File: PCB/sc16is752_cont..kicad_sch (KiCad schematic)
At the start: 57 parts, among them IC13 SN74LVC1G125DBVT, IC14 LM3940IMP-3.3_NOPB, IC15 SN74LVC1G125DBVT, IC16 AP63205WU-7, J3 5747842-2, J4 Screw_Terminal_01x02, J5 Screw_Terminal_01x02, J6 5747842-2, Q1 SI2307CDS-T1-GE3, Y2 ASE-14.7456MHZ-LC-T

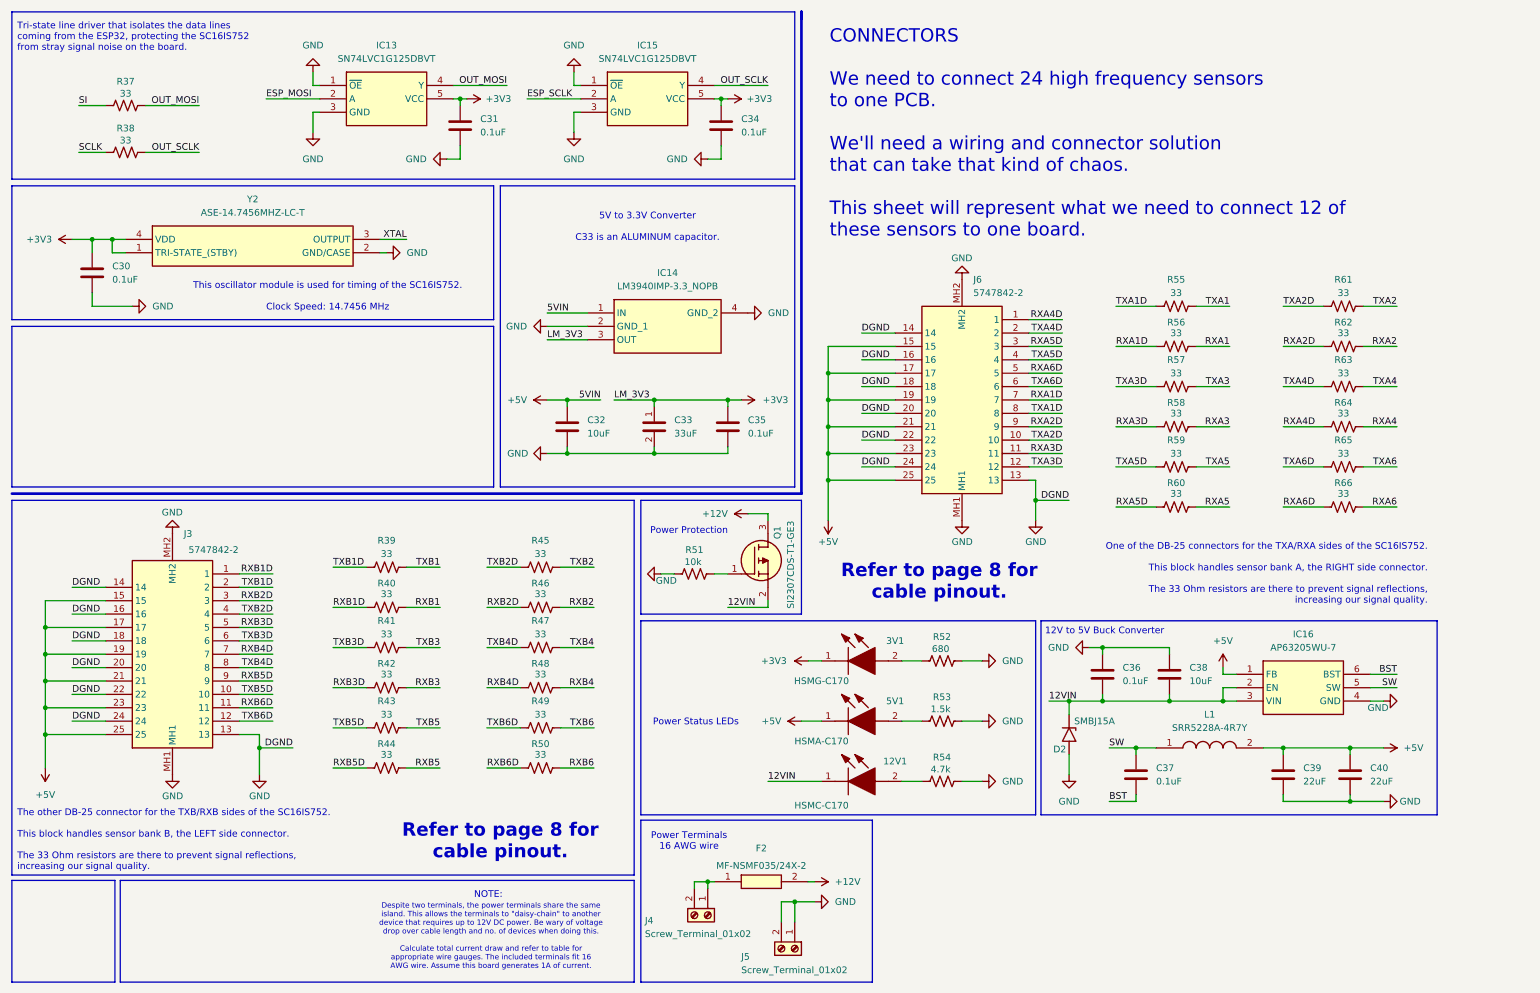
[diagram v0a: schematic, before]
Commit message: Add footprints & datasheets; clean PCB file
Add numerous component datasheets to PCB/Datasheets and introduce new footprints (DarkMagic:SRN2010BTA3R3M and DarkMagic:1812L010DR). Remove many redundant KiLib_Generator properties and perform footprint edits across the board including placement/rotation changes, pad orientation/net fixes, value and UUID updates, and silkscreen/fab text adjustments. Also add KiCad editor lock files (~DarkMagic.kicad_pcb.lck, ~DarkMagic.kicad_sch.lck).
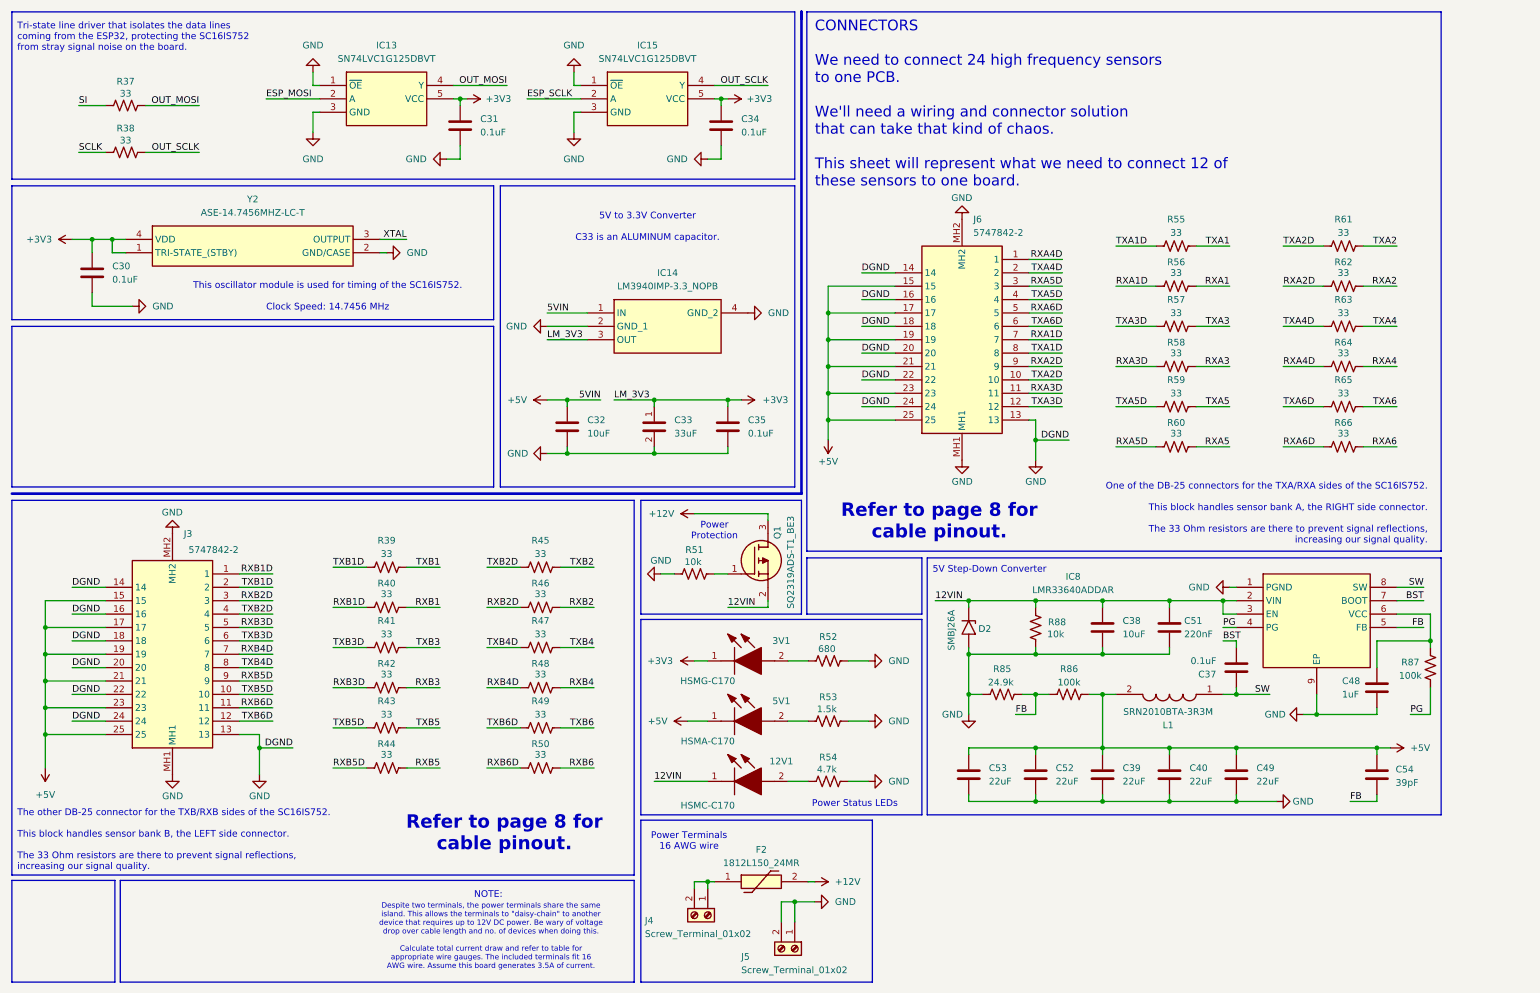
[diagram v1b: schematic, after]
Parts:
- removed C36: 0.1uF, Capacitor_SMD:C_0805_2012Metric_Pad1.18x1.45mm_HandSolder, symbol Device:C
- removed F2: MF-NSMF035/24X-2, Fuse:Fuse_1206_3216Metric_Pad1.42x1.75mm_HandSolder, symbol MF-MSMF250_16X-2:MF-MSMF250_16X-2
- removed IC16: AP63205WU-7, DarkMAgic:AP63205WU7, symbol AP63205WU-7:AP63205WU-7
- removed L1: SRR5228A-4R7Y, SRR5228A, symbol SRR5228A-4R7Y:SRR5228A-4R7Y
- added C48: 1uF, Capacitor_SMD:C_0805_2012Metric_Pad1.18x1.45mm_HandSolder, symbol Device:C
- added C49, C52, C53: 22uF, Capacitor_SMD:C_0805_2012Metric_Pad1.18x1.45mm_HandSolder, symbol Device:C
- added C51: 220nF, Capacitor_SMD:C_0805_2012Metric_Pad1.18x1.45mm_HandSolder, symbol Device:C
- added C54: 39pF, Capacitor_SMD:C_0805_2012Metric_Pad1.18x1.45mm_HandSolder, symbol Device:C
- added F2: 1812L150_24MR, 1812L010DR, symbol 1812L150_24MR:1812L150_24MR
- added IC8: LMR33640ADDAR, SOIC127P600X170-9N, symbol LMR33640ADDAR:LMR33640ADDAR
- added L1: SRN2010BTA-3R3M, SRN2010BTA3R3M, symbol SRN2010BTA-3R3M:SRN2010BTA-3R3M
- added R85: 24.9k, Resistor_SMD:R_0805_2012Metric_Pad1.20x1.40mm_HandSolder, symbol Device:R_US
- added R86, R87: 100k, Resistor_SMD:R_0805_2012Metric_Pad1.20x1.40mm_HandSolder, symbol Device:R_US
- added R88: 10k, Resistor_SMD:R_0805_2012Metric_Pad1.20x1.40mm_HandSolder, symbol Device:R_US
- C38: Manufacturer_Part_Number CL21A106KAYNNNF -> CL21A106KBYQNNE; Mouser Part Number 187-CL21A106KAYNNNF -> 187-CL21A106KBYQNNE
- D2: value SMBJ15A -> SMBJ26A; Manufacturer_Part_Number SMBJ15A -> SMBJ26A; Mouser Part Number 576-SMBJ15A -> 576-SMBJ26A
- Q1: value SI2307CDS-T1-GE3 -> SQ2319ADS-T1_BE3; Manufacturer_Part_Number Si2323DDS-T1-GE3 -> SQ2319ADS-T1_BE3; Mouser Part Number 78-SI2307CDS-T1-GE3 -> 78-SQ2319ADS-T1_BE3
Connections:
- net +12V: now also F2.2
- net +5V: now also C49.2, C52.2, C53.2, C54.1, L1.2, R86.2
- net 12VIN: now also C38.2, C51.2, IC8.2 (VIN), IC8.3 (EN), R88.2; no longer C38.1
- net BST: now also IC8.7 (BOOT)
- net GND: now also C38.1, C48.1, C49.1, C51.1, C52.1, C53.1, IC8.1 (PGND), IC8.9 (EP), R85.1, R88.1; no longer C38.2
- net SW: now also IC8.8 (SW), L1.1
- net at J4.1 (Pin_1), J4.2 (Pin_2): now also F2.1
- new net: C48.2, IC8.6 (VCC), R87.1
- new net FB: C54.2, IC8.5 (FB), R85.2, R86.1
- new net PG: IC8.4 (PG), R87.2
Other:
- note added: "5V Step-Down Converter"
- note added: "Despite two terminals, the power terminals share the same island. This allows the terminals to "daisy-chain" to another device that requires up to 12V DC power. Be wary of voltage drop over cable length and no. of devices when doing this. Calculate total current draw and refer to table for appropriate wire gauges. The included terminals fit 16 AWG wire. Assume this board generates 3.5A of current."
- note removed: "12V to 5V Buck Converter"
- note removed: "Despite two terminals, the power terminals share the same island. This allows the terminals to "daisy-chain" to another device that requires up to 12V DC power. Be wary of voltage drop over cable length and no. of devices when doing this. Calculate total current draw and refer to table for appropriate wire gauges. The included terminals fit 16 AWG wire. Assume this board generates 1A of current."
- moved on the sheet: 12V1, 3V1, 5V1, C37, C38, C39, C40, D2, J6, R52, R53, R54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

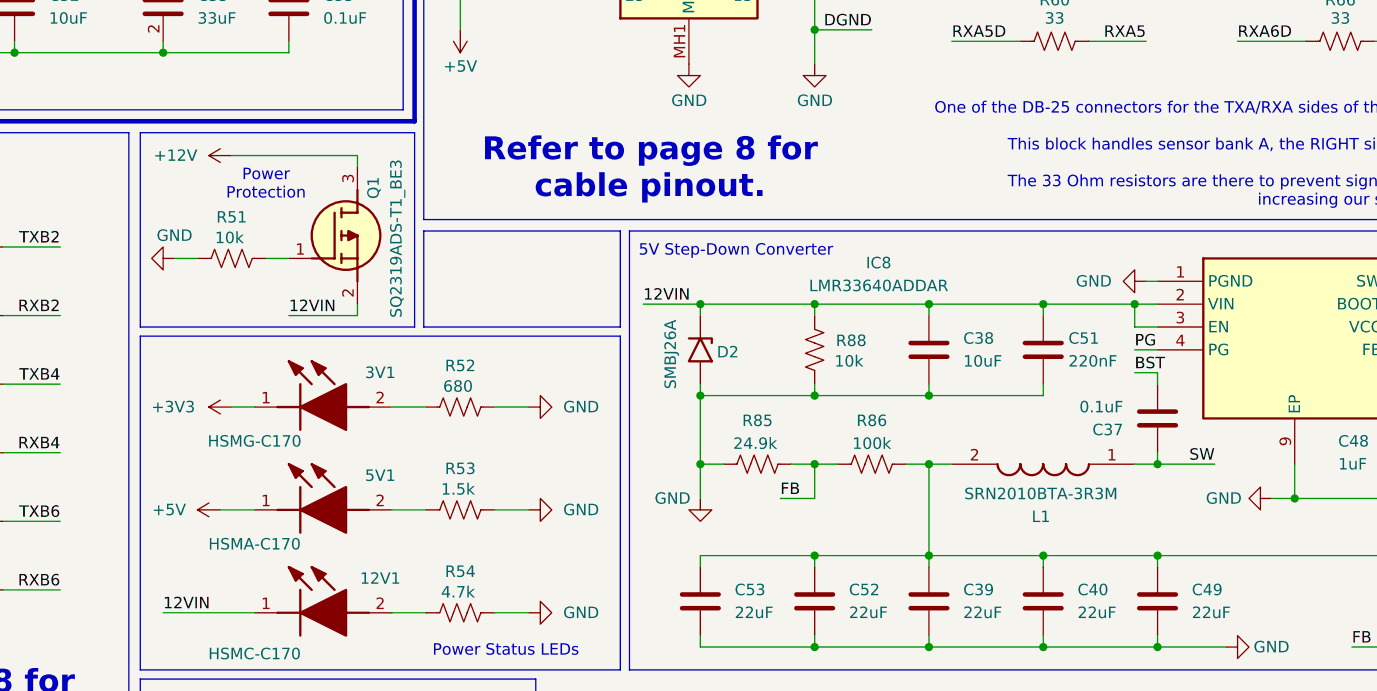
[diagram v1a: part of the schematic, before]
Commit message: Revise PCB footprints, nets and metadata
Refactor multiple footprints and metadata across the DarkMagic PCB files. Removed an obsolete SRN2010 inductor footprint and replaced a capacitor footprint with Inductor_SMD:L_12x12mm_H4.5mm (L1). Standardized net names (e.g. Net-(Q1-G) -> /Q1G), adjusted pad rotations/positions and many silkscreen/fab/crt geometry coordinates, and updated UUIDs and 3D model/part properties. Also updated component reference positions for a few ICs and capacitors and removed a stale KiCad schematic lock file. These edits clean up footprints, ensure consistent metadata and correct layout geometry for fabrication/assembly.
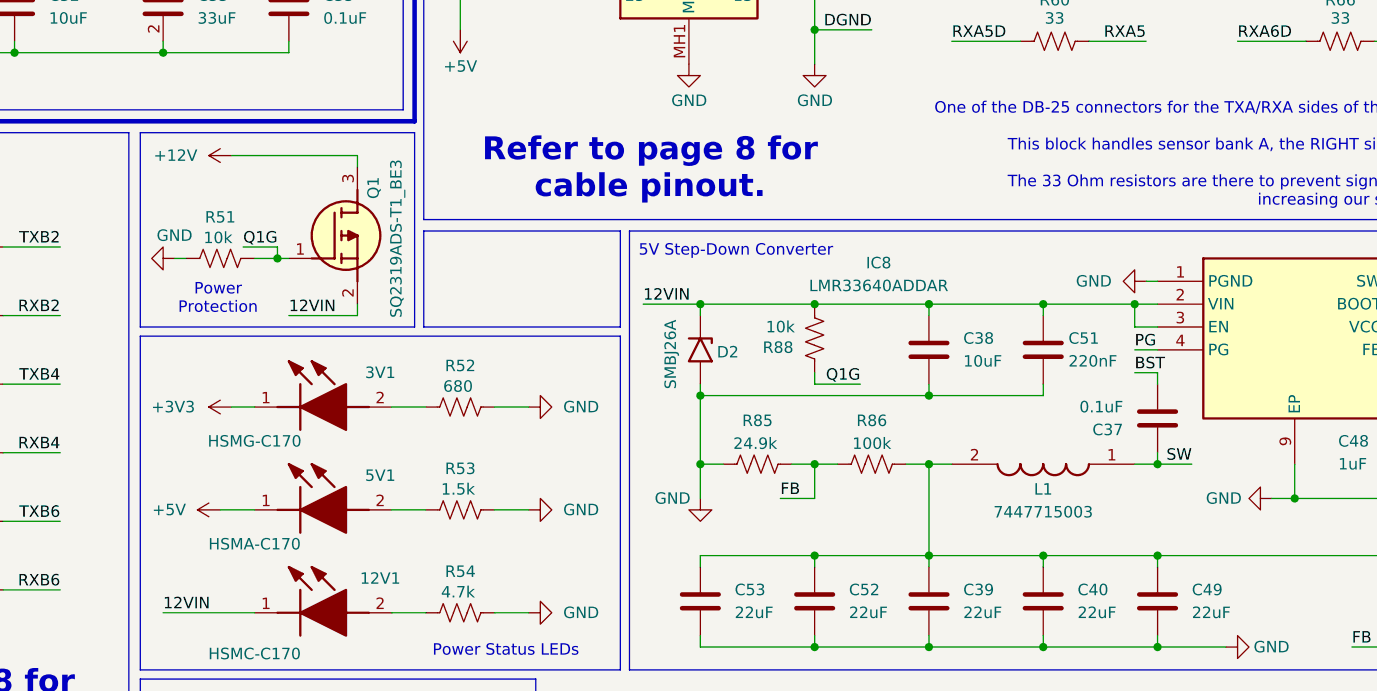
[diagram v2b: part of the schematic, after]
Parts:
- removed L1: SRN2010BTA-3R3M, SRN2010BTA3R3M, symbol SRN2010BTA-3R3M:SRN2010BTA-3R3M
- added L1: 7447715003, Inductor_SMD:L_12x12mm_H4.5mm, symbol 7447715003:7447715003
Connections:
- net +5V: now also L1.2
- net 12VIN: now also R88.1; no longer R88.2
- net GND: no longer R88.1
- net SW: now also L1.1
- net Q1G: now reaches Q1.1 (G), R51.2
- net Q1G: now also R88.2
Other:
- moved on the sheet: R51, R88

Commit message: Update BOM parts and adjust schematics text/layout
Apply multiple BOM updates and schematic edits: replace/update capacitor, diode, TVS, fuse, regulator, transistor, connector and resistor part numbers and quantities in DarkMagic.csv; add new components (C48/C51/C54, R85-R87, etc.). Change board active layer in DarkMagic.kicad_prl (9 -> 0). Update manufacturer/mouser part numbers for decoupling caps in esp32.kicad_sch and sc16is752_cont..kicad_sch. Tweak sheet text positions/fonts and remove a sentence in sc16is752_cont..kicad_sch, and add a printable installer-sign text block to sensor_pinout.kicad_sch for cable verification. These edits reflect revised part selections and improve schematic documentation/readability.
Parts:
- C32: Manufacturer_Part_Number CL21A106KAYNNNF -> CL21A106KBYQNNE; Mouser Part Number 187-CL21A106KAYNNNF -> 187-CL21A106KBYQNNE
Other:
- note added: "CONNECTORS We need to connect 24 high frequency sensors to one PCB. We'll need a wiring and connector solution that can take that kind of chaos."
- note removed: "CONNECTORS We need to connect 24 high frequency sensors to one PCB. We'll need a wiring and connector solution that can take that kind of chaos. This sheet will represent what we need to connect 12 of these sensors to one board."
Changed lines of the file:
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@@
 		)
 	)
-	(text "CONNECTORS\n\nWe need to connect 24 high frequency sensors\nto one PCB.\n\nWe'll need a wiring and connector solution \nthat can take that kind of chaos.\n\nThis sheet will represent what we need to connect 12 of\nthese sensors to one board."
+	(text "CONNECTORS\n\nWe need to connect 24 high frequency sensors\nto one PCB.\n\nWe'll need a wiring and connector solution \nthat can take that kind of chaos."
 		(exclude_from_sim no)
-		(at 165.1 30.226 0)
+		(at 165.1 28.702 0)
 		(effects
 			(font
-				(size 2.032 2.032)
+				(size 2.54 2.54)
 			)
 			(justify left)
@@
 	(text "Power Status LEDs"
 		(exclude_from_sim no)
-		(at 180.848 163.068 0)
+		(at 177.546 163.068 0)
 		(effects
 			(font
@@
 			)
 		)
-		(property "Manufacturer_Part_Number" "CL21A106KAYNNNF "
+		(property "Manufacturer_Part_Number" "CL21A106KBYQNNE"
 			(at 118.11 91.44 0)
 			(hide yes)
@@
 			)
 		)
-		(property "Mouser Part Number" "187-CL21A106KAYNNNF "
+		(property "Mouser Part Number" "187-CL21A106KBYQNNE "
 			(at 118.11 91.44 0)
 			(hide yes)
